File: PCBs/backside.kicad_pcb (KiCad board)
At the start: 2 copper layers, 147.3 x 110.5 mm, 66 parts, among them J1 9Pin, J14 Conn_01x07_Male, J15 Conn_01x07_Male, J16 Conn_01x07_Male, J17 Conn_01x04_Male, J18 Conn_02x17_Odd_Even, J3 Power, J4 Conn_01x17_Male, J5 Matrix, J6 Conn_01x17_Male, J7 Driver output 2, J8 Conn_01x04_Male, J9 Conn_01x30_Male, U1 HT1632C-52LQFP, U2 HT1632C-52LQFP, U3 STM32F103C8T6

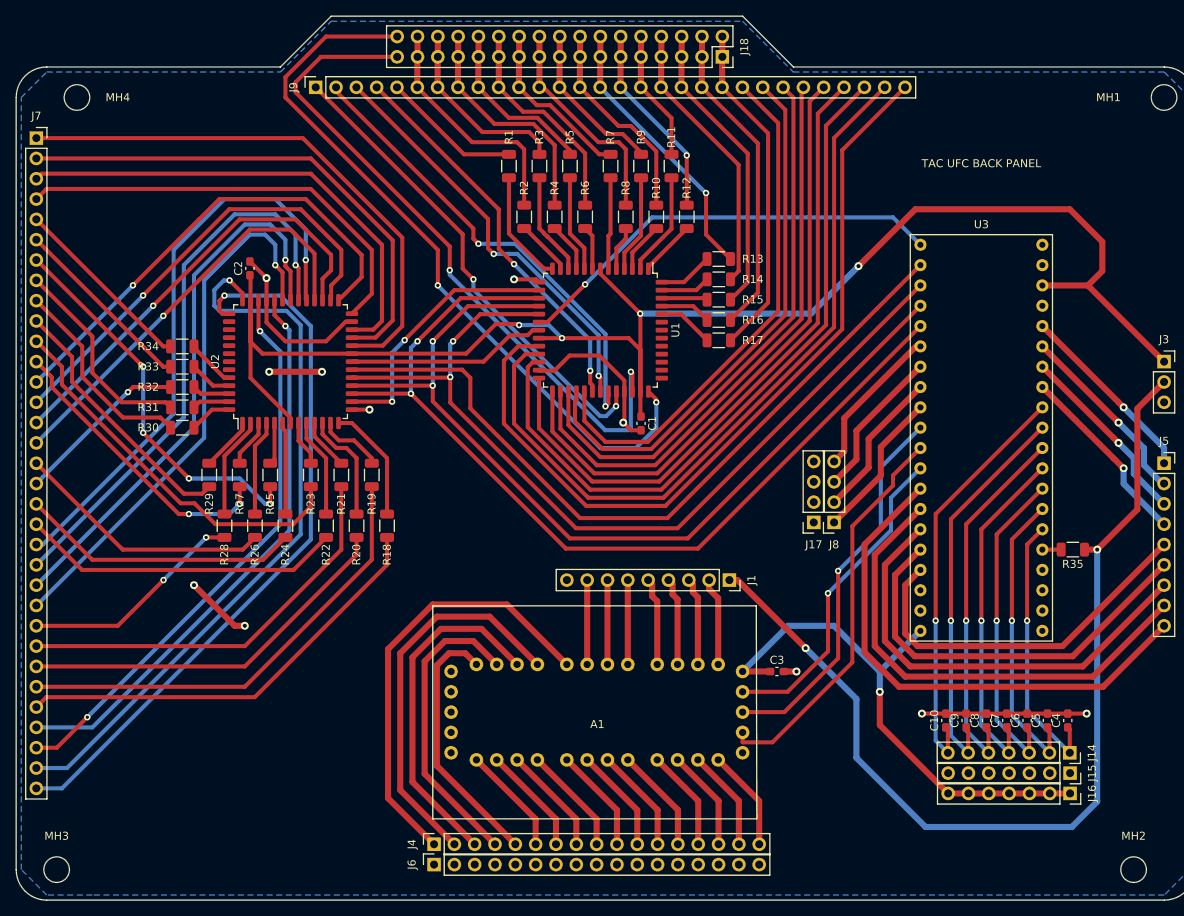
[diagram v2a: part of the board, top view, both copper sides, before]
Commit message: Updated silkscreen, fixed minor issues
Updated silkscreen to include pin designations, and fixed minor issue with ground plane
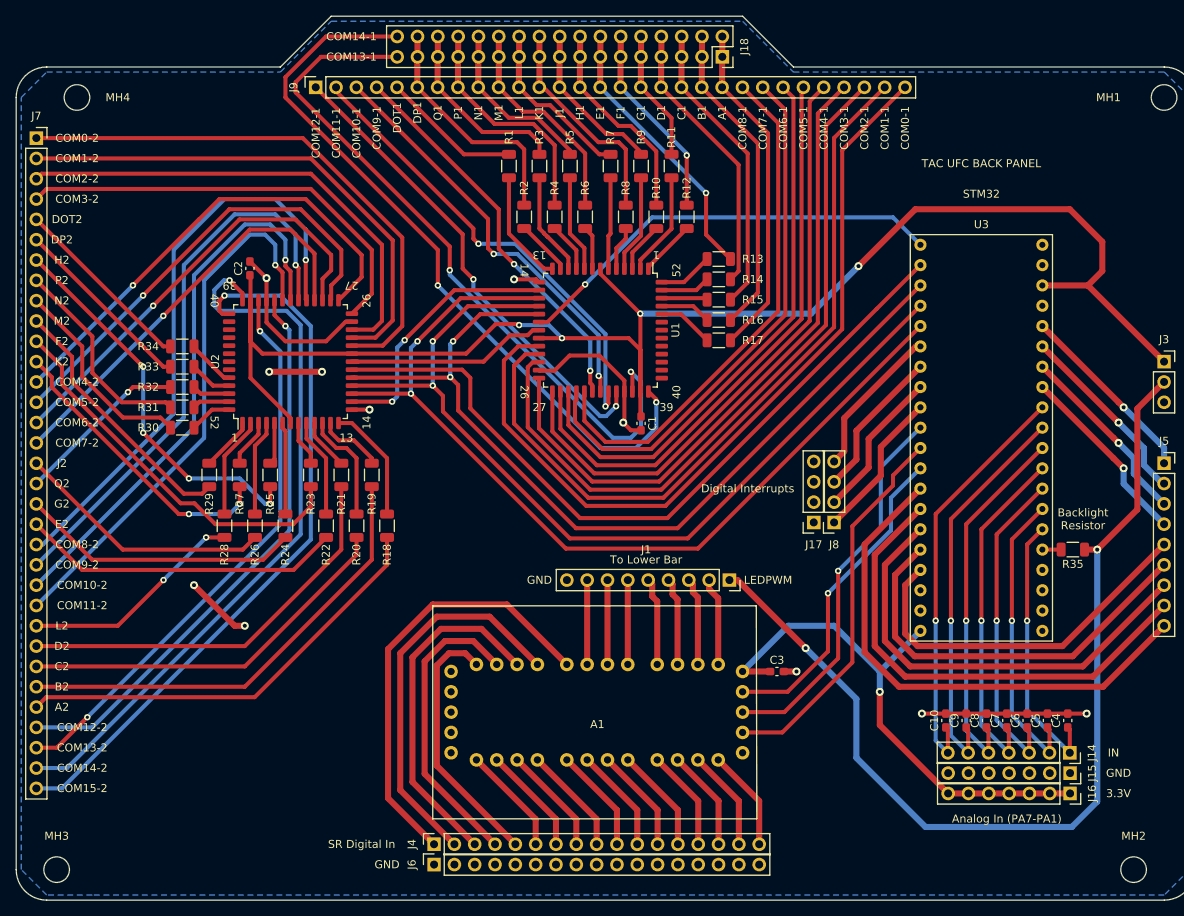
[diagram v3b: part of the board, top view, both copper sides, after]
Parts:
- R1, R10, R11, R12, R13, R14, R15, R16, R17, R18, R19, R2, R20, R21, R22, R23, R24, R25, R26, R27, R28, R29, R3, R30, R31, R32, R33, R34, R4, R5, R6, R7, R8, R9: value 520R -> 510R
- R35: value ? -> 100R
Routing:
- net /COM13-1: track 86.4 -> 89.0 mm
- net /SRCLK: track 49.4 -> 47.7 mm
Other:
- board text added: "1"
- board text added: "13"
- board text added: "14"
- board text added: "26"
- board text added: "27"
- board text added: "3.3V"
- board text added: "39"
- board text added: "40"
- board text added: "52"
- board text added: "A1"
- board text added: "A2"
- board text added: "Analog In (PA7-PA1)"
- board text added: "B1"
- board text added: "B2"
- board text added: "Backlight Resistor"
- board text added: "C1"
- board text added: "C2"
- board text added: "CC-BY-NC-SA"
- board text added: "COL1"
- board text added: "COL2"
- board text added: "COL3"
- board text added: "COL4"
- board text added: "COM0-1"
- board text added: "COM0-2"
- board text added: "COM1-1"
- board text added: "COM1-2"
- board text added: "COM10-1"
- board text added: "COM10-2"
- board text added: "COM11-1"
- board text added: "COM11-2"
- board text added: "COM12-1"
- board text added: "COM12-2"
- board text added: "COM13-1"
- board text added: "COM13-2"
- board text added: "COM14-1"
- board text added: "COM14-2"
- board text added: "COM15-2"
- board text added: "COM2-1"
- board text added: "COM2-2"
- board text added: "COM3-1"
- board text added: "COM3-2"
- board text added: "COM4-1"
- board text added: "COM4-2"
- board text added: "COM5-1"
- board text added: "COM5-2"
- board text added: "COM6-1"
- board text added: "COM6-2"
- board text added: "COM7-1"
- board text added: "COM7-2"
- board text added: "COM8-1"
- board text added: "COM8-2"
- board text added: "COM9-1"
- board text added: "COM9-2"
- board text added: "D1"
- board text added: "D2"
- board text added: "DOT1"
- board text added: "DOT2"
- board text added: "DP1"
- board text added: "DP2"
- board text added: "Digital Interrupts"
- board text added: "E1"
- board text added: "E2"
- board text added: "F1"
- board text added: "F2"
- board text added: "G1"
- board text added: "G2"
- board text added: "GND"
- board text added: "H1"
- board text added: "H2"
- board text added: "IN"
- board text added: "J1"
- board text added: "J2"
- board text added: "K1"
- board text added: "K2"
- board text added: "L1"
- board text added: "L2"
- board text added: "LEDPWM"
- board text added: "M1"
- board text added: "M2"
- board text added: "N1"
- board text added: "N2"
- board text added: "P1"
- board text added: "P2"
- board text added: "Q1"
- board text added: "Q2"
- board text added: "ROW0"
- board text added: "ROW1"
- board text added: "ROW2"
- board text added: "ROW3"
- board text added: "ROW4"
- board text added: "SR Digital In"
- board text added: "STM32"
- board text added: "To Lower Bar"

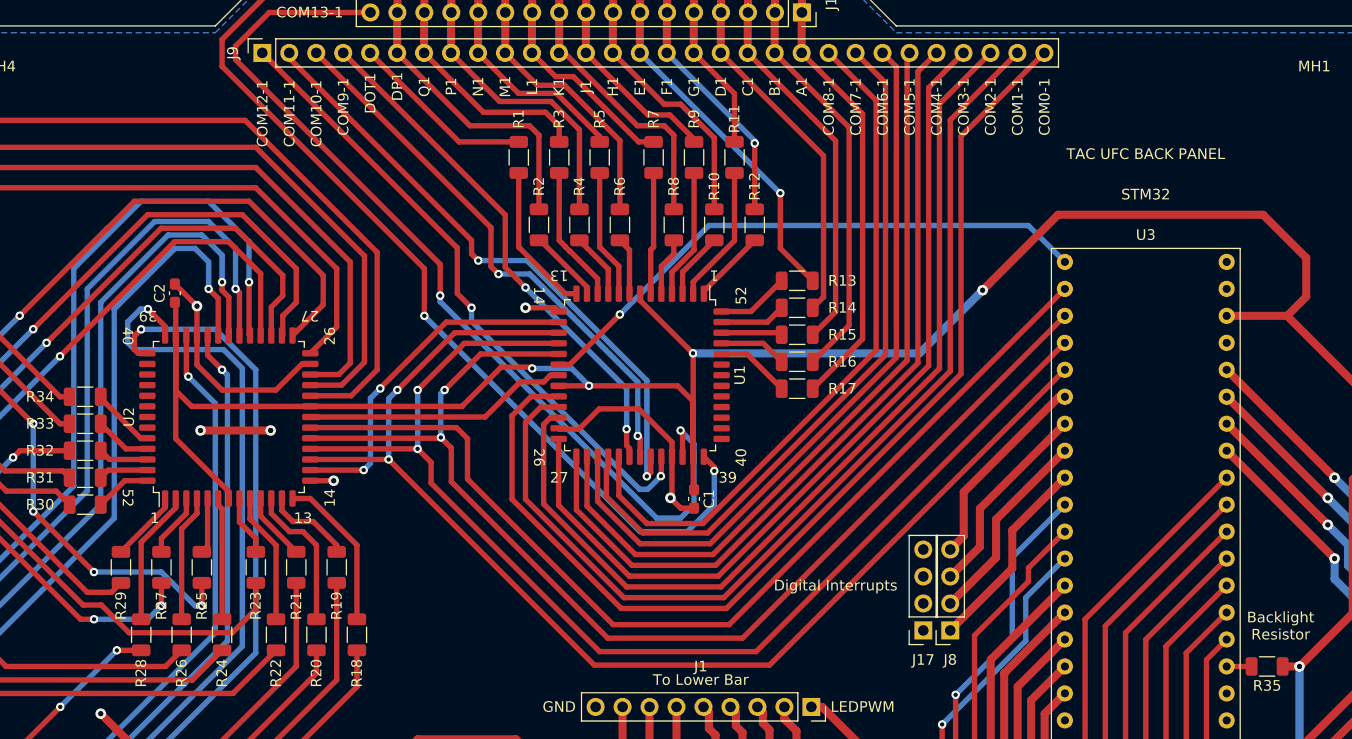
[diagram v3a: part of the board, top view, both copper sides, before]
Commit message: Removed comm displays from PCB
Since they will be connected with wires anyways it didn't make sense to keep them on.
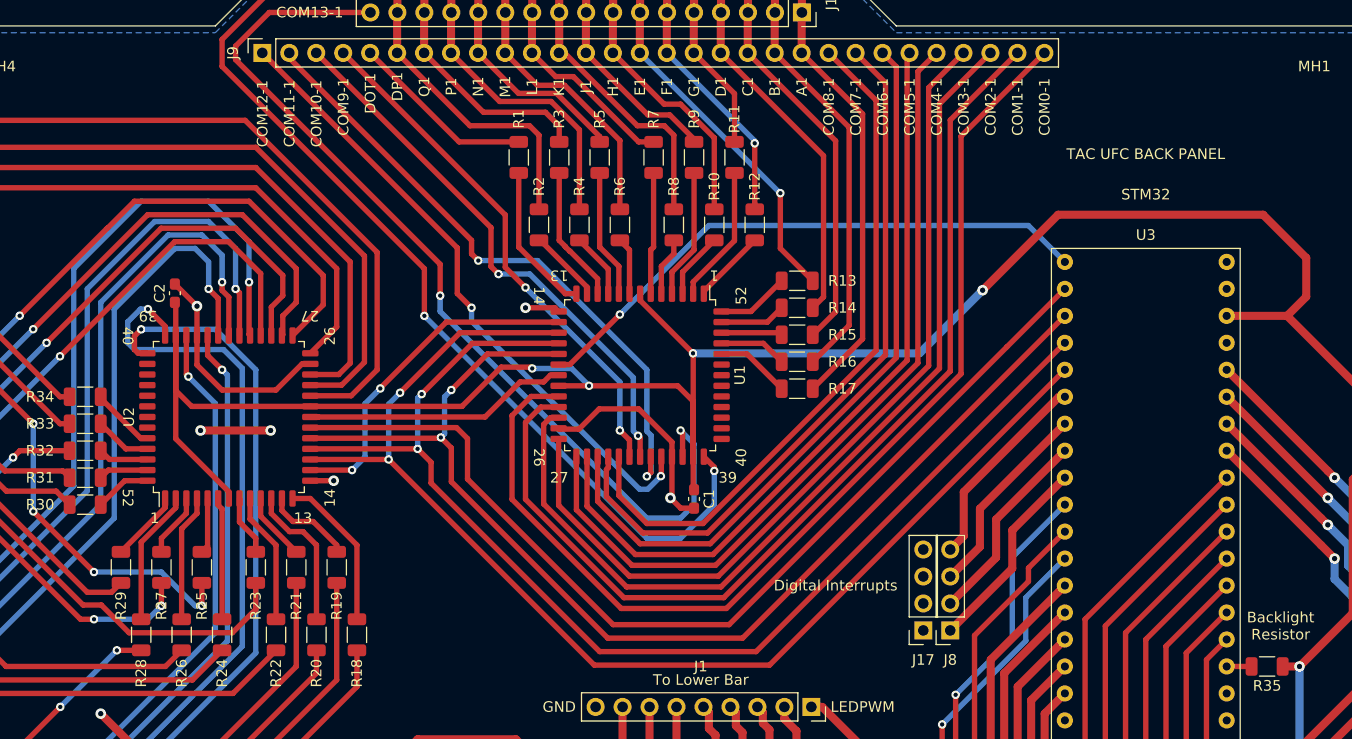
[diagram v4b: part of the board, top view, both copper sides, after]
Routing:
- net /COM11-1: track 58.5 -> 59.4 mm
- net /OSC: track 32.8 -> 32.1 mm
- net /COM13-1: track 89.0 -> 89.5 mm
- net /COM14-1: track 91.7 -> 92.2 mm

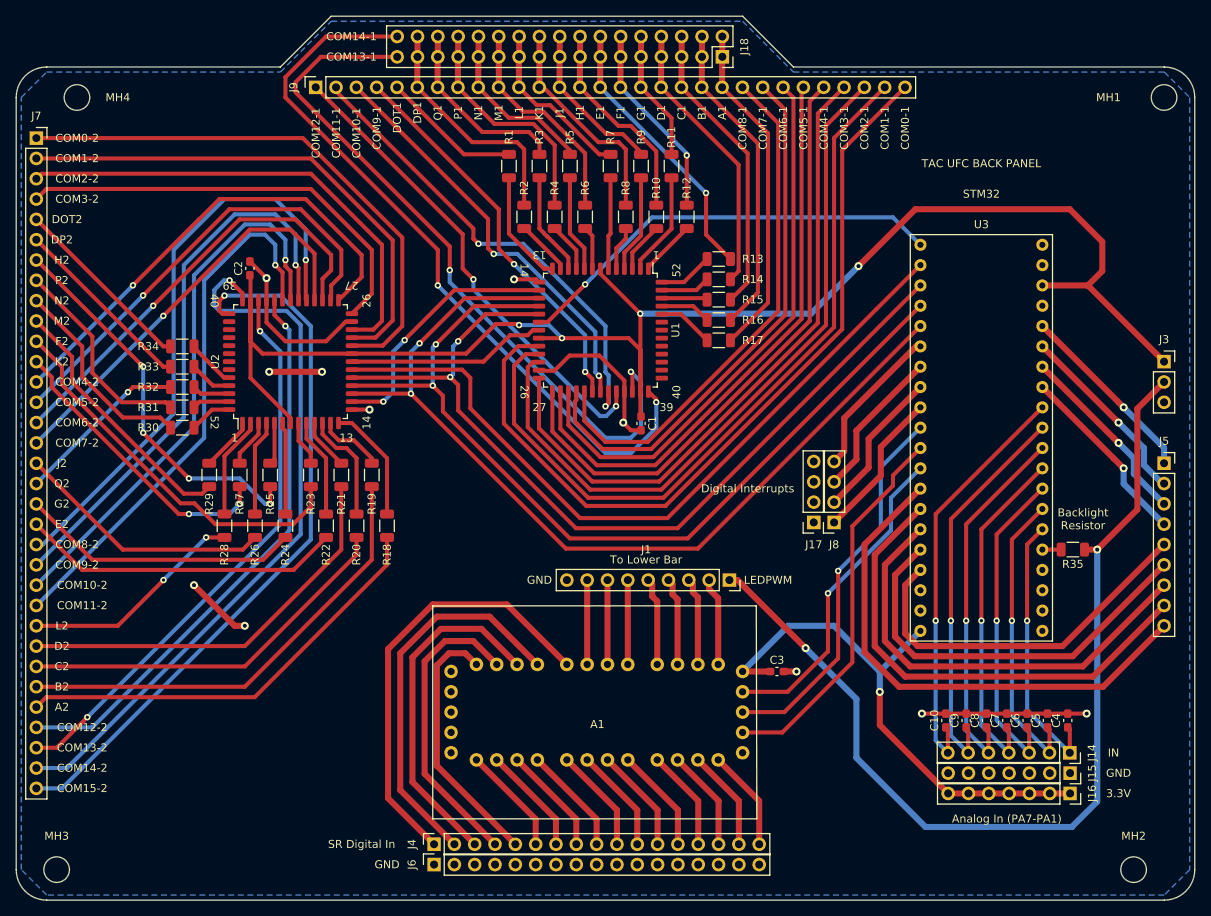
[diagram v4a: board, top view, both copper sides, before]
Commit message: Updated PCBs, cleaned up files
No commit for a while; a lot has happened in the mean time. JLC refused my order for the display layers, so I settled for just the dot layer. The gerbers for the rest are deleted, but the kicad files are still present.

I also received the main PCBs from JLC, and edited a couple small details.
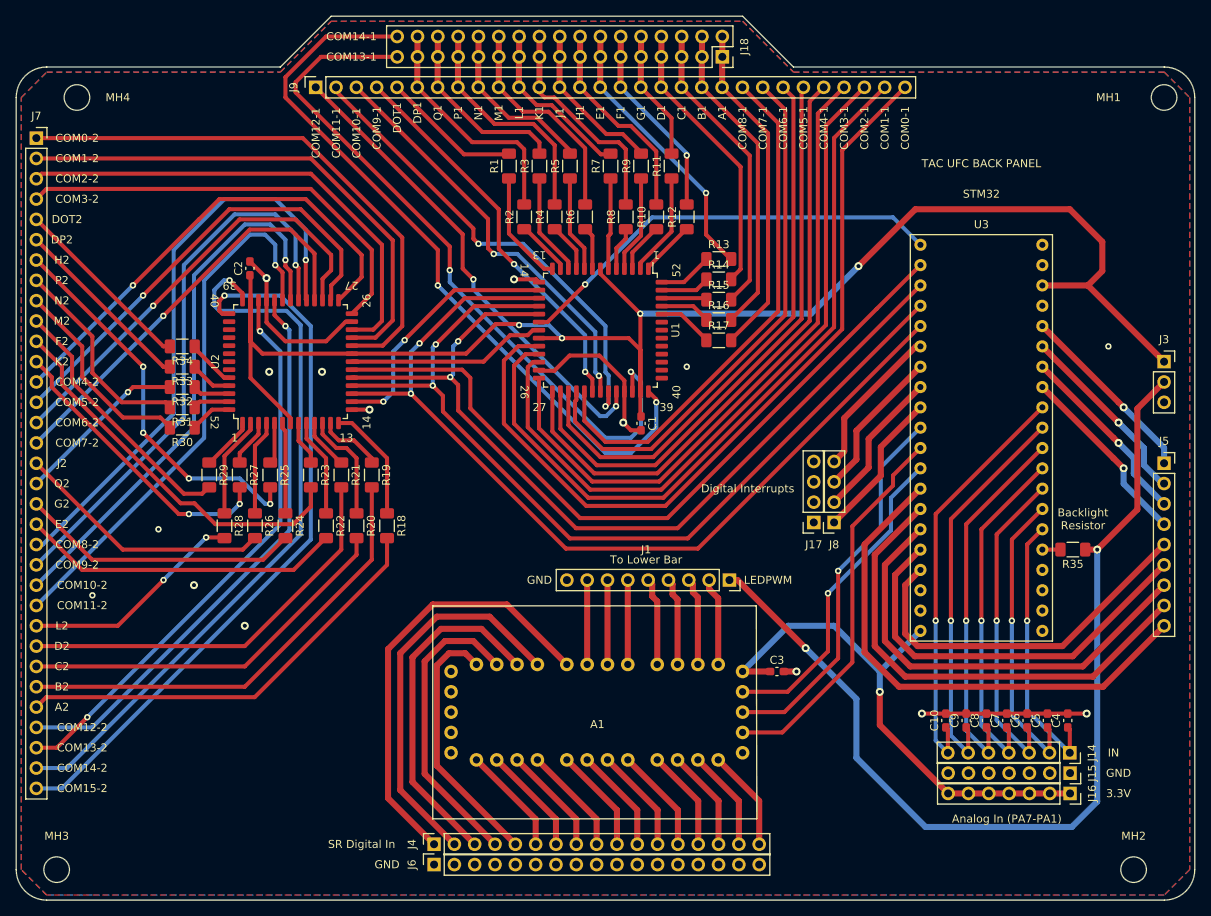
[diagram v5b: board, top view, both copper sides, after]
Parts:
- R1, R10, R11, R12, R13, R14, R15, R16, R17, R18, R19, R2, R20, R21, R22, R23, R24, R25, R26, R27, R28, R29, R3, R30, R31, R32, R33, R34, R35, R4, R5, R6, R7, R8, R9: footprint Resistor_SMD:R_1206_3216Metric -> Resistor_SMD:R_1206_3216Metric_Pad1.30x1.75mm_HandSolder
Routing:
- net /GND: track 84.6 -> 69.5 mm, vias 11 -> 15
- added copper zone on F.Cu, net /GND
